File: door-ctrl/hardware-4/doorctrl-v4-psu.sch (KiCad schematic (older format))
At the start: 30 parts, among them U2 MC34063, U3 L4960

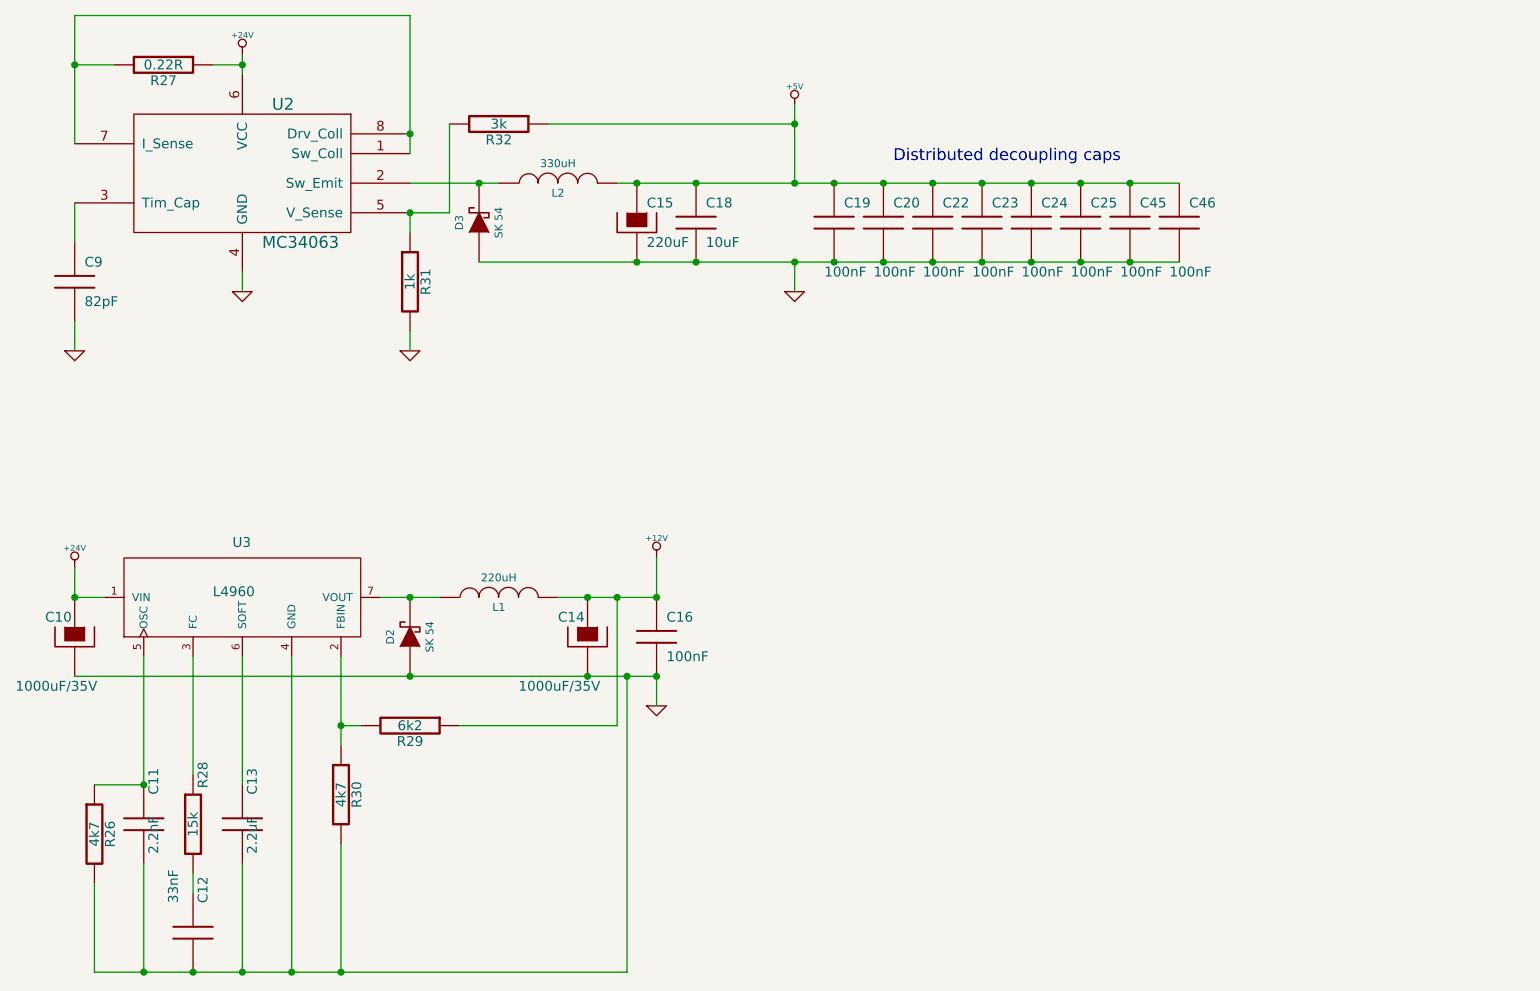
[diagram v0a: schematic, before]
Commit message: Did various cleanups, added mounting holes to the schematic, so they don't disappear and grounded them, removed the redundant levelshifter
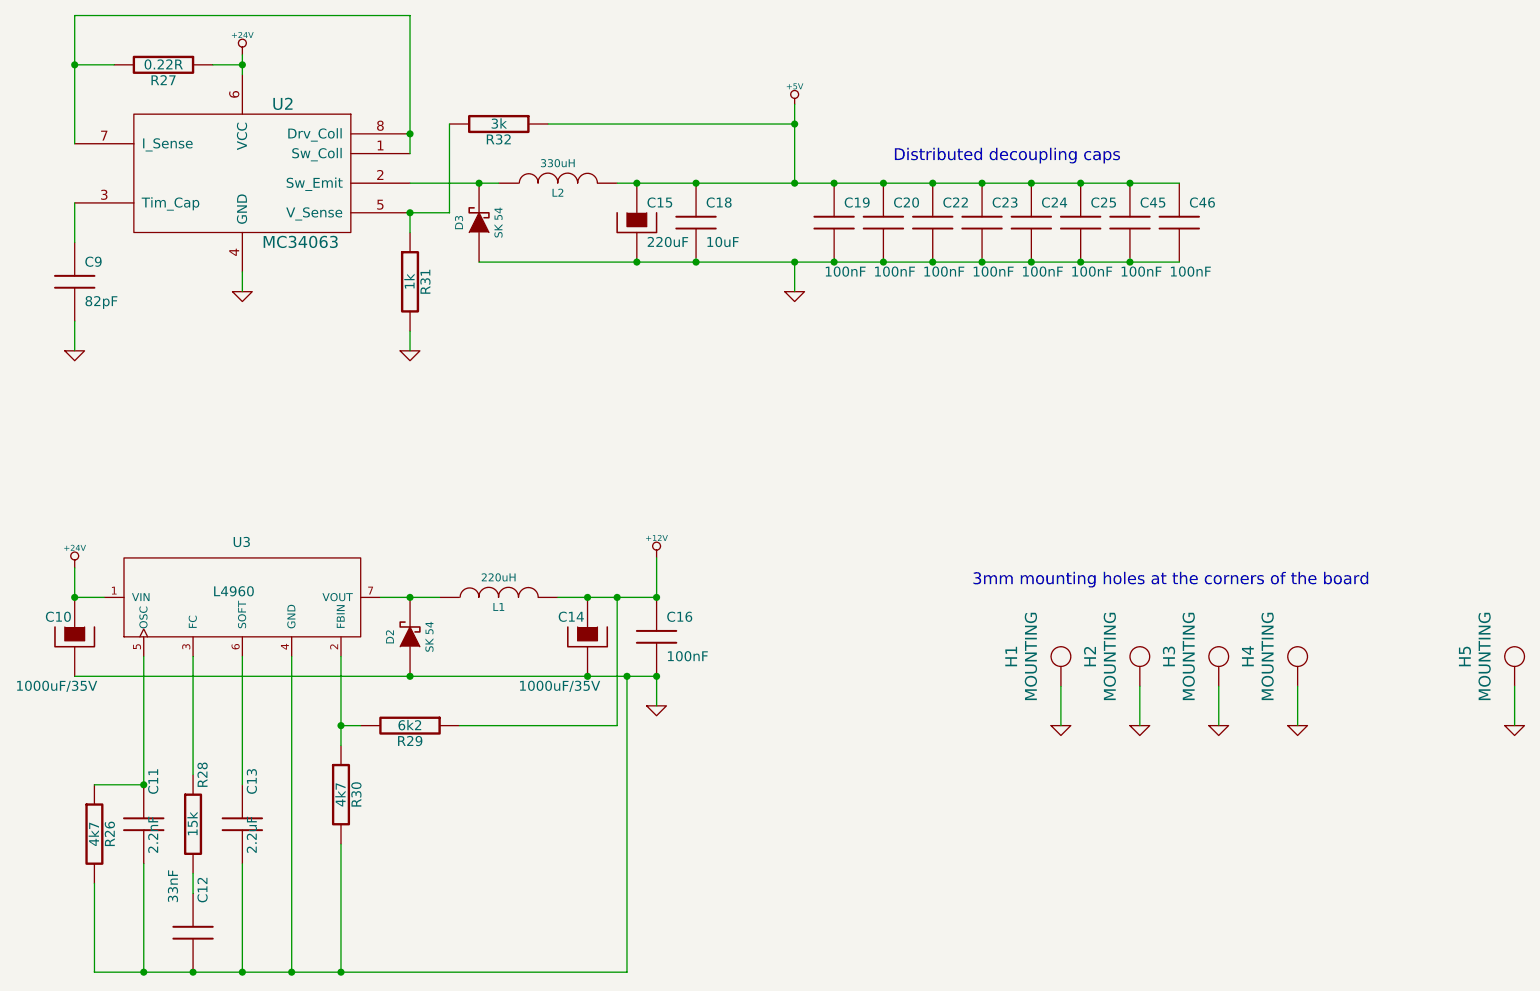
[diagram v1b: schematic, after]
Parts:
- added H1, H2, H3, H4, H5: MOUNTING, symbol MOUNTING
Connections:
- net GND: now also H1.1 (hole), H2.1 (hole), H3.1 (hole), H4.1 (hole), H5.1 (hole)
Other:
- note added: "3mm mounting holes at the corners of the board"
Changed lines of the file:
@@
-EESchema Schematic File Version 2  date 2011-03-10T21:41:37 CET
+EESchema Schematic File Version 2  date 2011-03-21T20:05:08 CET
 LIBS:enc28j60
 LIBS:power
@@
 LIBS:diode
 LIBS:npnpnp
+LIBS:mounting
 LIBS:doorctrl-v4-cache
 EELAYER 25  0
@@
 Sheet 6 6
 Title ""
-Date "4 feb 2011"
+Date "21 mar 2011"
 Rev ""
 Comp ""
@@
 Comment4 ""
 $EndDescr
+Wire Wire Line
+	9500 5150 9500 5350
+Wire Wire Line
+	8000 5150 8000 5350
+Wire Wire Line
+	7200 5150 7200 5350
+Wire Wire Line
+	4250 3000 7800 3000
+Wire Wire Line
+	4150 5350 4950 5350
+Connection ~ 3550 5350
+Wire Wire Line
+	3650 5350 3550 5350
+Connection ~ 5150 5100
+Connection ~ 5150 4700
+Connection ~ 2200 4700
+Connection ~ 2550 5650
+Wire Wire Line
+	3750 4700 4050 4700
+Wire Wire Line
+	2200 4550 2200 4700
+Wire Wire Line
+	2200 5100 5150 5100
+Wire Wire Line
+	5000 5100 5000 6600
+Wire Wire Line
+	5000 6600 2300 6600
+Wire Wire Line
+	2800 5600 2800 5000
+Connection ~ 3050 6600
+Wire Wire Line
+	3050 6050 3050 6600
+Connection ~ 3550 6600
+Wire Wire Line
+	5150 5100 5150 5250
+Connection ~ 3900 5100
+Wire Wire Line
+	5150 4500 5150 4700
+Connection ~ 2800 6600
+Connection ~ 2550 6600
+Wire Wire Line
+	2550 6050 2550 6600
+Wire Wire Line
+	2300 5650 2550 5650
+Wire Wire Line
+	5850 2600 5850 2200
+Connection ~ 5850 3000
+Wire Wire Line
+	5850 3000 5850 3150
+Connection ~ 7300 2600
+Connection ~ 6800 2600
+Connection ~ 6050 2600
+Connection ~ 6550 3000
+Connection ~ 7050 3000
+Connection ~ 6050 3000
+Connection ~ 5850 2300
+Connection ~ 5050 2600
+Wire Wire Line
+	4600 2300 5850 2300
+Connection ~ 4250 2600
+Wire Wire Line
+	4350 2600 3900 2600
+Connection ~ 3900 2750
+Wire Wire Line
+	3900 2850 3900 2750
+Wire Wire Line
+	3900 3350 3900 3450
+Wire Wire Line
+	2200 3300 2200 3450
+Connection ~ 3050 2000
+Wire Wire Line
+	2900 2000 3050 2000
+Connection ~ 3900 2350
+Wire Wire Line
+	3900 2450 3900 1750
+Wire Wire Line
+	3050 1950 3050 2050
+Wire Wire Line
+	2200 2400 2200 1750
+Wire Wire Line
+	2200 1750 3900 1750
+Wire Wire Line
+	2400 2000 2200 2000
+Connection ~ 2200 2000
+Wire Wire Line
+	2200 2900 2200 2700
+Wire Wire Line
+	3050 3050 3050 3150
+Wire Wire Line
+	3900 2750 4100 2750
+Wire Wire Line
+	4100 2750 4100 2300
+Connection ~ 5350 2600
+Connection ~ 5050 3000
+Connection ~ 5350 3000
+Connection ~ 6300 3000
+Connection ~ 6800 3000
+Connection ~ 7300 3000
+Connection ~ 6300 2600
+Connection ~ 6550 2600
+Connection ~ 7050 2600
+Connection ~ 5850 2600
+Wire Wire Line
+	2300 6600 2300 6150
+Wire Wire Line
+	2800 6100 2800 6200
+Connection ~ 3900 4700
+Wire Wire Line
+	5150 4700 4650 4700
+Connection ~ 4800 4700
+Connection ~ 4800 5100
+Connection ~ 5000 5100
+Connection ~ 4950 4700
+Wire Wire Line
+	3050 5650 3050 5000
+Wire Wire Line
+	2550 5650 2550 5000
+Wire Wire Line
+	3300 5000 3300 6600
+Connection ~ 3300 6600
+Wire Wire Line
+	2200 4700 2350 4700
+Wire Wire Line
+	3550 5450 3550 5000
+Wire Wire Line
+	3550 5950 3550 6600
+Wire Wire Line
+	4950 5350 4950 4700
+Connection ~ 7550 2600
+Connection ~ 7550 3000
+Wire Wire Line
+	7800 2600 4950 2600
+Wire Wire Line
+	7600 5150 7600 5350
+Wire Wire Line
+	8400 5150 8400 5350
+$Comp
+L GND #PWR073
+U 1 1 4D879ADC
+P 9500 5350
+F 0 "#PWR073" H 9500 5350 30  0001 C CNN
+F 1 "GND" H 9500 5280 30  0001 C CNN
+	1    9500 5350
+	1    0    0    -1
+$EndComp
+$Comp
+L MOUNTING H5
+U 1 1 4D879AD2
+P 9500 5000
+F 0 "H5" H 9500 5250 60  0000 C CNN
+F 1 "MOUNTING" H 9500 5150 60  0000 C CNN
+	1    9500 5000
+	0    -1   -1   0
+$EndComp
+Text Notes 6750 4650 0    60   ~ 0
+3mm mounting holes at the corners of the board
+$Comp
+L GND #PWR074
+U 1 1 4D87999F
+P 8400 5350
+F 0 "#PWR074" H 8400 5350 30  0001 C CNN
+F 1 "GND" H 8400 5280 30  0001 C CNN
+	1    8400 5350
+	1    0    0    -1
+$EndComp
+$Comp
+L GND #PWR075
+U 1 1 4D87999A
+P 8000 5350
+F 0 "#PWR075" H 8000 5350 30  0001 C CNN
+F 1 "GND" H 8000 5280 30  0001 C CNN
+	1    8000 5350
+	1    0    0    -1
+$EndComp
+$Comp
+L GND #PWR076
+U 1 1 4D879997
+P 7600 5350
+F 0 "#PWR076" H 7600 5350 30  0001 C CNN
+F 1 "GND" H 7600 5280 30  0001 C CNN
+	1    7600 5350
+	1    0    0    -1
+$EndComp
+$Comp
+L GND #PWR077
+U 1 1 4D879990
+P 7200 5350
+F 0 "#PWR077" H 7200 5350 30  0001 C CNN
+F 1 "GND" H 7200 5280 30  0001 C CNN
+	1    7200 5350
+	1    0    0    -1
+$EndComp
+$Comp
+L MOUNTING H4
+U 1 1 4D879985
+P 8400 5000
+F 0 "H4" H 8400 5250 60  0000 C CNN
+F 1 "MOUNTING" H 8400 5150 60  0000 C CNN
+	1    8400 5000
+	0    -1   -1   0
+$EndComp
+$Comp
+L MOUNTING H3
+U 1 1 4D87997E
+P 8000 5000
+F 0 "H3" H 8000 5250 60  0000 C CNN
+F 1 "MOUNTING" H 8000 5150 60  0000 C CNN
+	1    8000 5000
+	0    -1   -1   0
+$EndComp
+$Comp
+L MOUNTING H2
+U 1 1 4D879975
+P 7600 5000
+F 0 "H2" H 7600 5250 60  0000 C CNN
+F 1 "MOUNTING" H 7600 5150 60  0000 C CNN
+	1    7600 5000
+	0    -1   -1   0
+$EndComp
+$Comp
+L MOUNTING H1
+U 1 1 4D87996B
+P 7200 5000
+F 0 "H1" H 7200 5250 60  0000 C CNN
+F 1 "MOUNTING" H 7200 5150 60  0000 C CNN
+	1    7200 5000
+	0    -1   -1   0
+$EndComp
 Text Notes 6350 2500 0    60   ~ 0
 Distributed decoupling caps
-Wire Wire Line
-	7800 2600 4950 2600
-Connection ~ 7550 3000
-Connection ~ 7550 2600
-Wire Wire Line
-	4950 4700 4950 5350
-Wire Wire Line
-	3550 5950 3550 6600
-Wire Wire Line
-	3550 5450 3550 5000
-Wire Wire Line
-	2350 4700 2200 4700
-Connection ~ 3300 6600
-Wire Wire Line
-	3300 5000 3300 6600
-Wire Wire Line
-	2550 5000 2550 5650
-Wire Wire Line
-	3050 5650 3050 5000
-Connection ~ 4950 4700
-Connection ~ 5000 5100
-Connection ~ 4800 5100
-Connection ~ 4800 4700
-Wire Wire Line
-	4650 4700 5150 4700
-Connection ~ 3900 4700
-Wire Wire Line
-	2800 6100 2800 6200
-Wire Wire Line
-	2300 6150 2300 6600
-Connection ~ 5850 2600
-Connection ~ 7050 2600
-Connection ~ 6550 2600
-Connection ~ 6300 2600
-Connection ~ 7300 3000
-Connection ~ 6800 3000
-Connection ~ 6300 3000
-Connection ~ 5350 3000
-Connection ~ 5050 3000
-Connection ~ 5350 2600
-Wire Wire Line
-	4100 2300 4100 2750
-Wire Wire Line
-	4100 2750 3900 2750
-Wire Wire Line
-	3050 3050 3050 3150
-Wire Wire Line
-	2200 2900 2200 2700
-Connection ~ 2200 2000
-Wire Wire Line
-	2400 2000 2200 2000
-Wire Wire Line
-	2200 1750 3900 1750
-Wire Wire Line
-	2200 1750 2200 2400
-Wire Wire Line
-	3050 1950 3050 2050
-Wire Wire Line
-	3900 1750 3900 2450
-Connection ~ 3900 2350
-Wire Wire Line
-	2900 2000 3050 2000
-Connection ~ 3050 2000
-Wire Wire Line
-	2200 3300 2200 3450
-Wire Wire Line
-	3900 3350 3900 3450
-Wire Wire Line
-	3900 2750 3900 2850
-Connection ~ 3900 2750
-Wire Wire Line
-	4350 2600 3900 2600
-Connection ~ 4250 2600
-Wire Wire Line
-	4600 2300 5850 2300
-Connection ~ 5050 2600
-Connection ~ 5850 2300
-Connection ~ 6050 3000
-Connection ~ 7050 3000
-Connection ~ 6550 3000
-Connection ~ 6050 2600
-Connection ~ 6800 2600
-Connection ~ 7300 2600
-Wire Wire Line
-	5850 3000 5850 3150
-Connection ~ 5850 3000
-Wire Wire Line
-	5850 2600 5850 2200
-Wire Wire Line
-	2550 5650 2300 5650
-Wire Wire Line
-	2550 6050 2550 6600
-Connection ~ 2550 6600
-Connection ~ 2800 6600
-Wire Wire Line
-	5150 4700 5150 4500
-Connection ~ 3900 5100
-Wire Wire Line
-	5150 5250 5150 5100
-Connection ~ 3550 6600
-Wire Wire Line
-	3050 6050 3050 6600
-Connection ~ 3050 6600
-Wire Wire Line
-	2800 5600 2800 5000
-Wire Wire Line
-	2300 6600 5000 6600
-Wire Wire Line
-	5000 6600 5000 5100
-Wire Wire Line
-	5150 5100 2200 5100
-Wire Wire Line
-	2200 4700 2200 4550
-Wire Wire Line
-	3750 4700 4050 4700
-Connection ~ 2550 5650
-Connection ~ 2200 4700
-Connection ~ 5150 4700
-Connection ~ 5150 5100
-Wire Wire Line
-	3650 5350 3550 5350
-Connection ~ 3550 5350
-Wire Wire Line
-	4950 5350 4150 5350
-Wire Wire Line
-	4250 3000 7800 3000
 $Comp
 L C C46
@@
 $EndComp
 $Comp
-L +5V #PWR076
+L +5V #PWR078
 U 1 1 4D0BB423
 P 5850 2200
-F 0 "#PWR076" H 5850 2290 20  0001 C CNN
+F 0 "#PWR078" H 5850 2290 20  0001 C CNN
 F 1 "+5V" H 5850 2290 30  0000 C CNN
 	1    5850 2200
@@
 $EndComp
 $Comp
-L GND #PWR077
+L GND #PWR079
 U 1 1 4D04D8EB
 P 5150 5250
-F 0 "#PWR077" H 5150 5250 30  0001 C CNN
+F 0 "#PWR079" H 5150 5250 30  0001 C CNN
 F 1 "GND" H 5150 5180 30  0001 C CNN
 	1    5150 5250
@@
 $EndComp
 $Comp
-L +12V #PWR078
+L +12V #PWR080
 U 1 1 4D04D8CC
 P 5150 4500
-F 0 "#PWR078" H 5150 4450 20  0001 C CNN
+F 0 "#PWR080" H 5150 4450 20  0001 C CNN
 F 1 "+12V" H 5150 4600 30  0000 C CNN
 	1    5150 4500
@@
 $EndComp
 $Comp
-L +24V #PWR079
+L +24V #PWR081
 U 1 1 4D04D7BB
 P 2200 4550
-F 0 "#PWR079" H 2200 4500 20  0001 C CNN
+F 0 "#PWR081" H 2200 4500 20  0001 C CNN
 F 1 "+24V" H 2200 4650 30  0000 C CNN
 	1    2200 4550
@@
 $EndComp
 $Comp
-L GND #PWR080
+L GND #PWR082
 U 1 1 4D04D42D
 P 5850 3150
-F 0 "#PWR080" H 5850 3150 30  0001 C CNN
+F 0 "#PWR082" H 5850 3150 30  0001 C CNN
 F 1 "GND" H 5850 3080 30  0001 C CNN
 	1    5850 3150
@@
 $EndComp
 $Comp
-L GND #PWR081
+L GND #PWR083
 U 1 1 4D04CF0D
 P 2200 3450
-F 0 "#PWR081" H 2200 3450 30  0001 C CNN
+F 0 "#PWR083" H 2200 3450 30  0001 C CNN
 F 1 "GND" H 2200 3380 30  0001 C CNN
 	1    2200 3450
@@
 $EndComp
 $Comp
-L GND #PWR082
+L GND #PWR084
 U 1 1 4D04CF06
 P 3900 3450
-F 0 "#PWR082" H 3900 3450 30  0001 C CNN
+F 0 "#PWR084" H 3900 3450 30  0001 C CNN
 F 1 "GND" H 3900 3380 30  0001 C CNN
 	1    3900 3450
@@
 $EndComp
 $Comp
-L GND #PWR083
+L GND #PWR085
 U 1 1 4D04CF02
 P 3050 3150
-F 0 "#PWR083" H 3050 3150 30  0001 C CNN
+F 0 "#PWR085" H 3050 3150 30  0001 C CNN
 F 1 "GND" H 3050 3080 30  0001 C CNN
 	1    3050 3150
@@
 $EndComp
 $Comp
-L +24V #PWR084
+L +24V #PWR086
 U 1 1 4D04CE42
 P 3050 1950
-F 0 "#PWR084" H 3050 1900 20  0001 C CNN
+F 0 "#PWR086" H 3050 1900 20  0001 C CNN
 F 1 "+24V" H 3050 2050 30  0000 C CNN
 	1    3050 1950
